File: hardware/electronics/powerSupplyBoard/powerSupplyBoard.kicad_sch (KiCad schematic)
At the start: 26 parts, among them J1 USB_C_Receptacle_USB2.0, SW1 PTS647, SW2 SS-12D07, U1 STM32L052K6, U2 AP2112K-3.3, Y1 ECS-327ATQMV

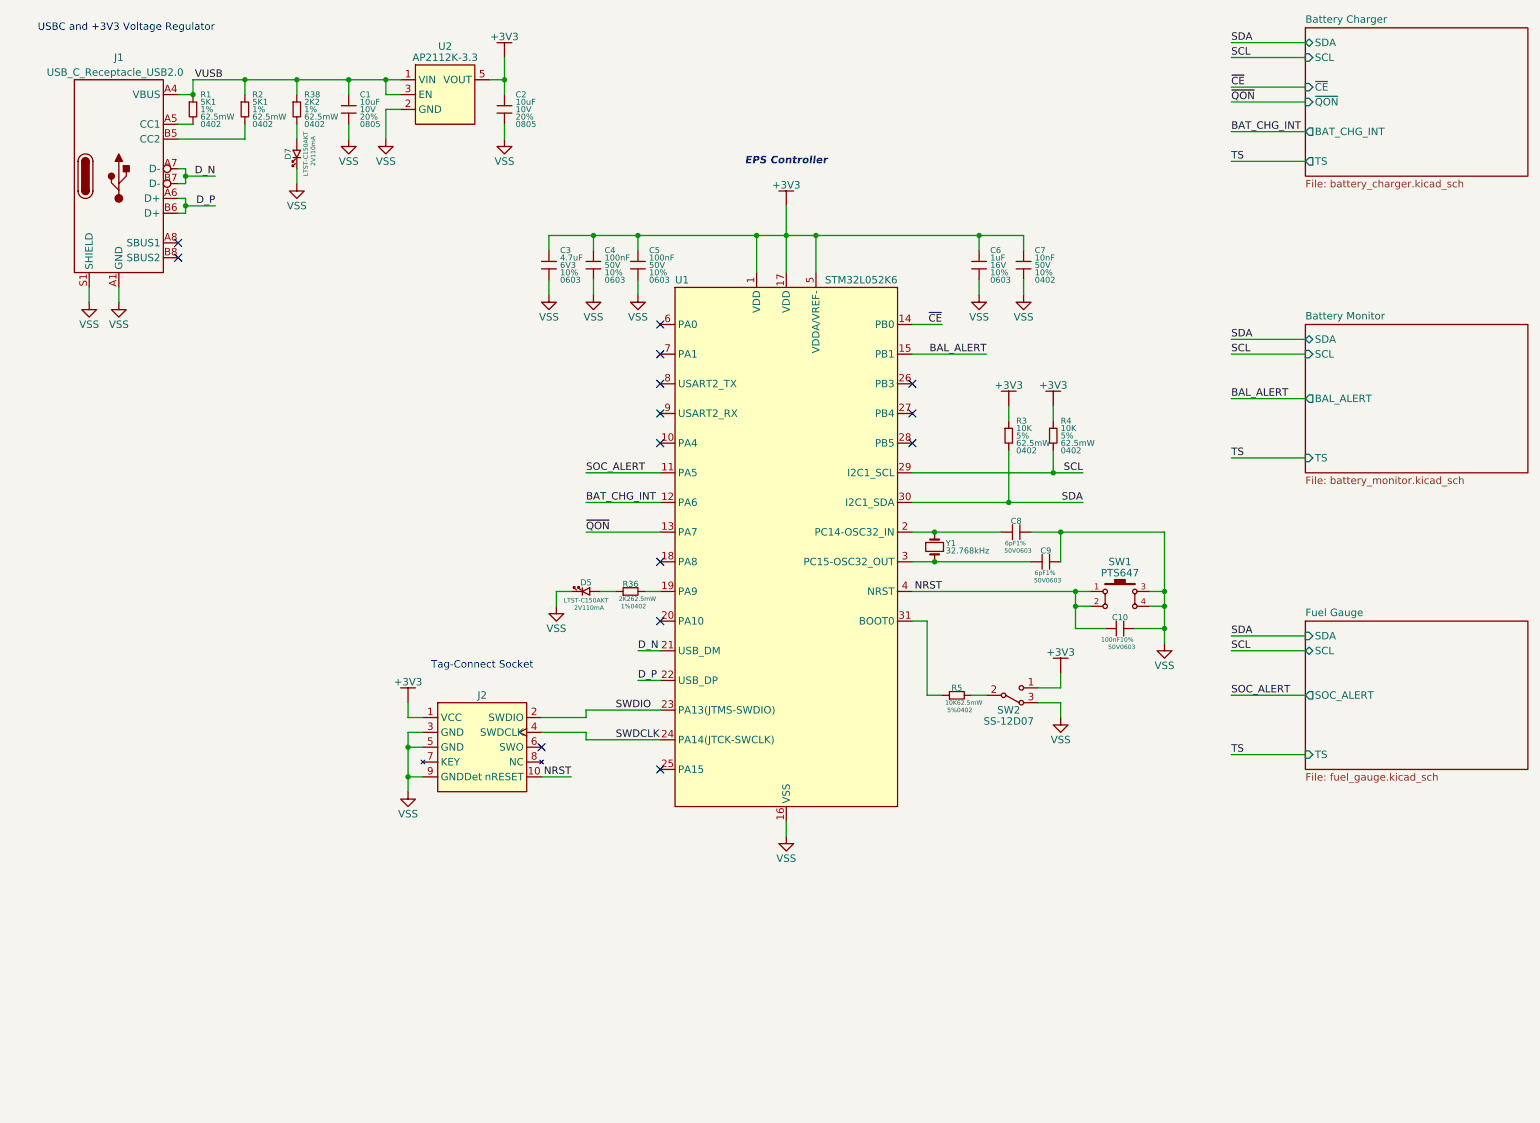
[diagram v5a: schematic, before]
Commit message: fixed USB resistors. updated sheet name and part refs
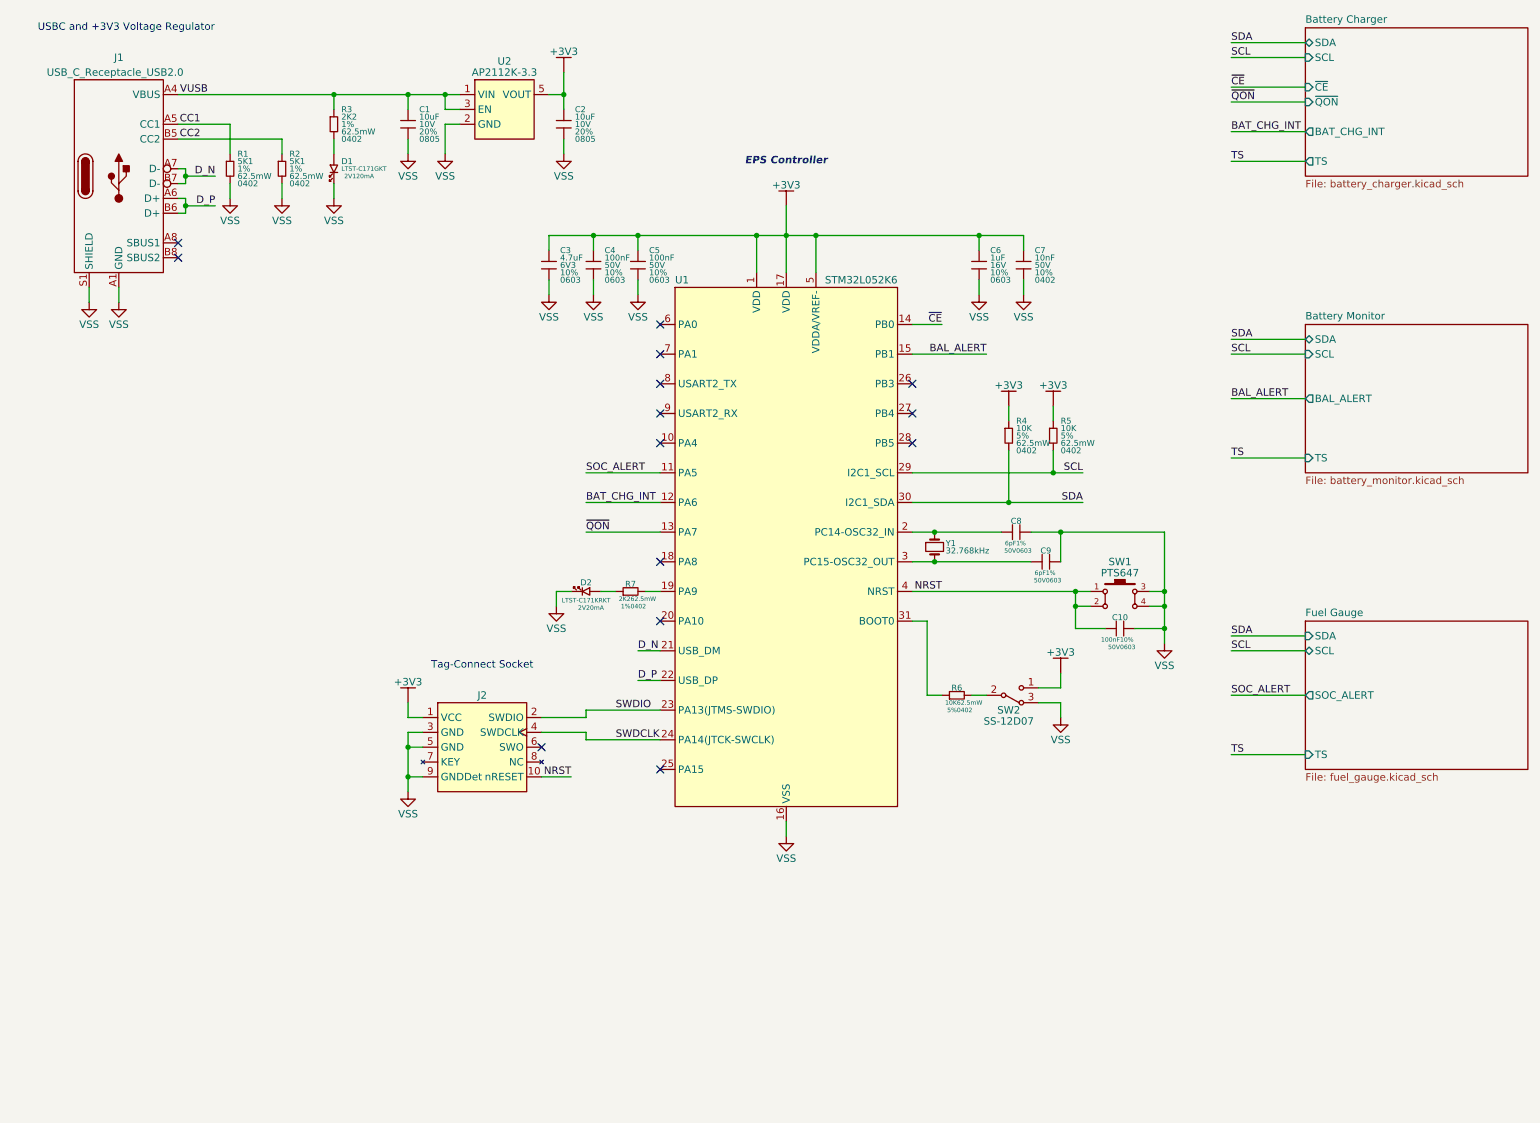
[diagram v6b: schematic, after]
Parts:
- D1: renamed from D7; value LTST-C150AKT -> LTST-C171GKT; footprint lib_fp:LTST-1206 -> lib_fp:LTST-0805; Current 10mA -> 20mA; DKPN 160-1166-1-ND -> 160-1423-1-ND; MPN LTST-C150AKT -> LTST-C171GKT
- D2: renamed from D5; value LTST-C150AKT -> LTST-C171KRKT; footprint lib_fp:LTST-1206 -> lib_fp:LTST-0805; Current 10mA -> 20mA; DKPN 160-1166-1-ND -> 160-1427-1-ND; Forward Voltage 2V1 -> 2V; MPN LTST-C150AKT -> LTST-C171KRKT
- renumbered R38 to R3, R3 to R4, R4 to R5, R5 to R6, R36 to R7
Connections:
- net VSS: now also R1.2, R2.2
- net VUSB: no longer R1.1, R2.1
- net CC1: now reaches J1.A5 (CC1)
- net CC1: now also R1.1; no longer R1.2
- net CC2: now reaches J1.B5 (CC2)
- net CC2: now also R2.1; no longer R2.2
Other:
- moved on the sheet: C1, C2, D1, R1, R2, R3, U2

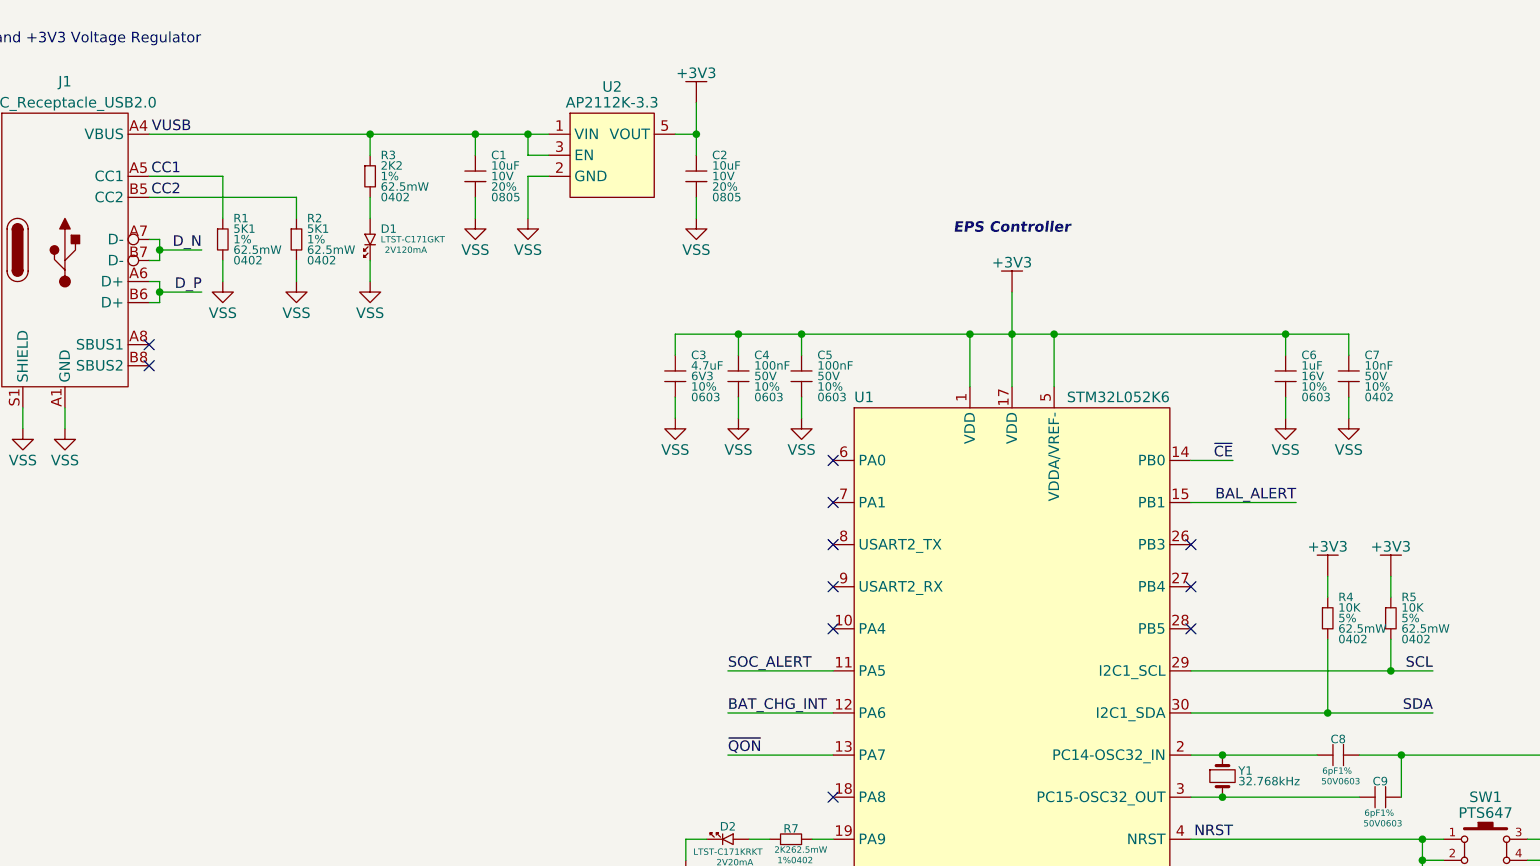
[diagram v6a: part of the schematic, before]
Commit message: added testpoints
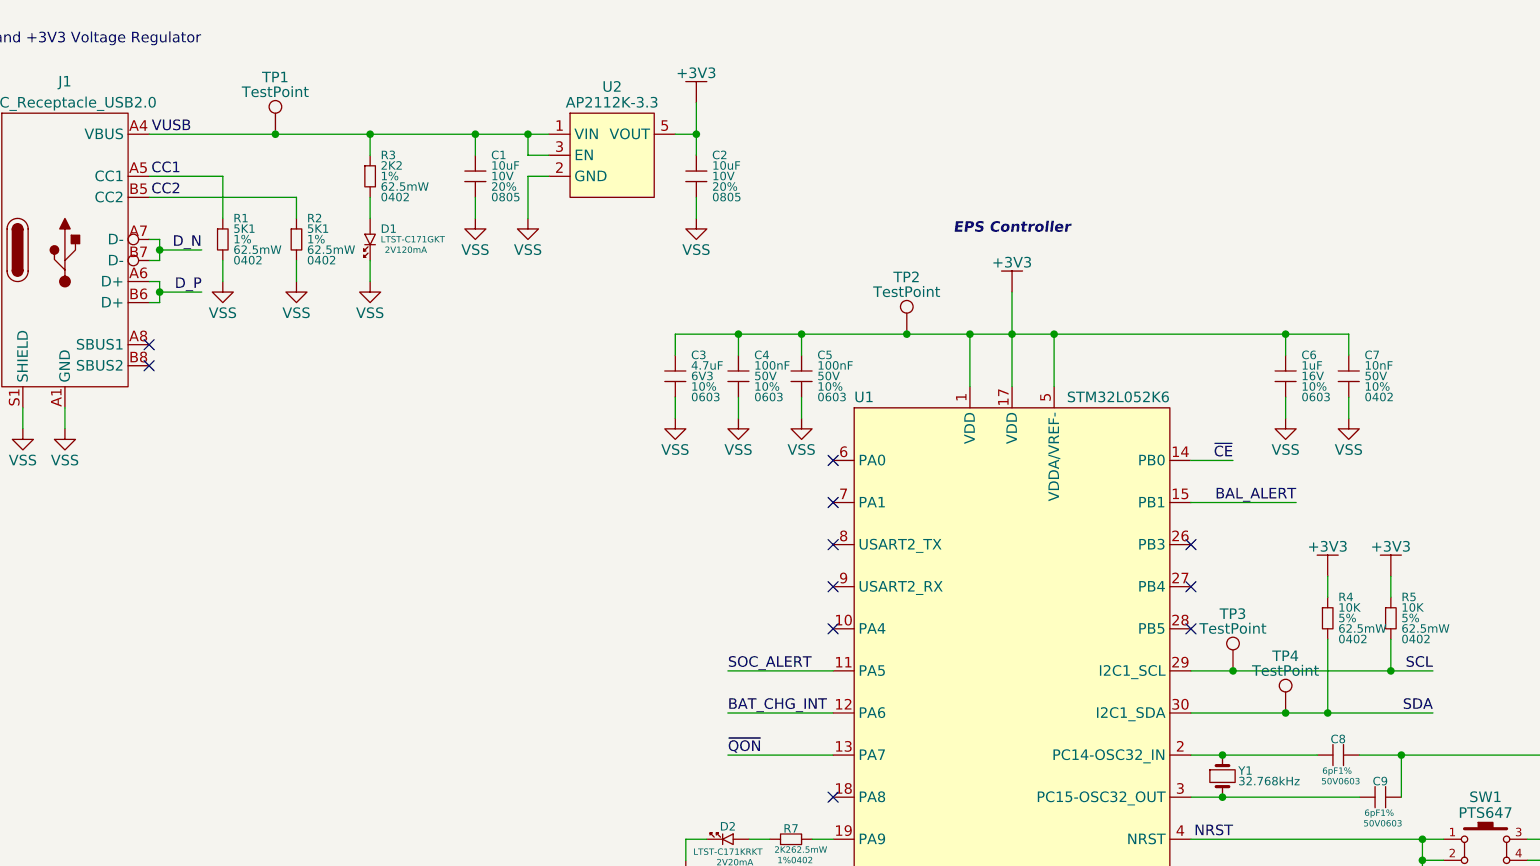
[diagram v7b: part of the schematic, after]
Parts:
- added TP1, TP2, TP3, TP4: TestPoint, lib_fp:TP_1mm, symbol lib_sch:TestPoint
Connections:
- net +3V3: now also TP2.1
- net SCL: now also TP3.1
- net SDA: now also TP4.1
- net VUSB: now also TP1.1

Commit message: cleaned up schematics
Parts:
- C3, C4, C5, C7: symbol lib_sch:C_2 -> lib_sch:C
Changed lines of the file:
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@@
 	(title_block
 		(title "Awohali Power Supply")
-		(date "2024-11-18")
+		(date "2024-11-20")
 		(rev "01")
 		(comment 2 "PROTOTYPE")
@@
 	)
 	(symbol
-		(lib_name "C_2")
-		(lib_id "lib_sch:C_2")
+		(lib_id "lib_sch:C")
 		(at 114.3 53.34 0)
 		(unit 1)
@@
 	)
 	(symbol
-		(lib_name "C_2")
-		(lib_id "lib_sch:C_2")
+		(lib_id "lib_sch:C")
 		(at 99.06 53.34 0)
 		(unit 1)
@@
 	)
 	(symbol
-		(lib_name "C_2")
-		(lib_id "lib_sch:C_2")
+		(lib_id "lib_sch:C")
 		(at 180.34 53.34 0)
 		(unit 1)
@@
 	)
 	(symbol
-		(lib_name "C_2")
-		(lib_id "lib_sch:C_2")
+		(lib_id "lib_sch:C")
 		(at 106.68 53.34 0)
 		(unit 1)
